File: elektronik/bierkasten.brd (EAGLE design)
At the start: 160 x 100 mm, 71 parts, among them Q1 BC547B

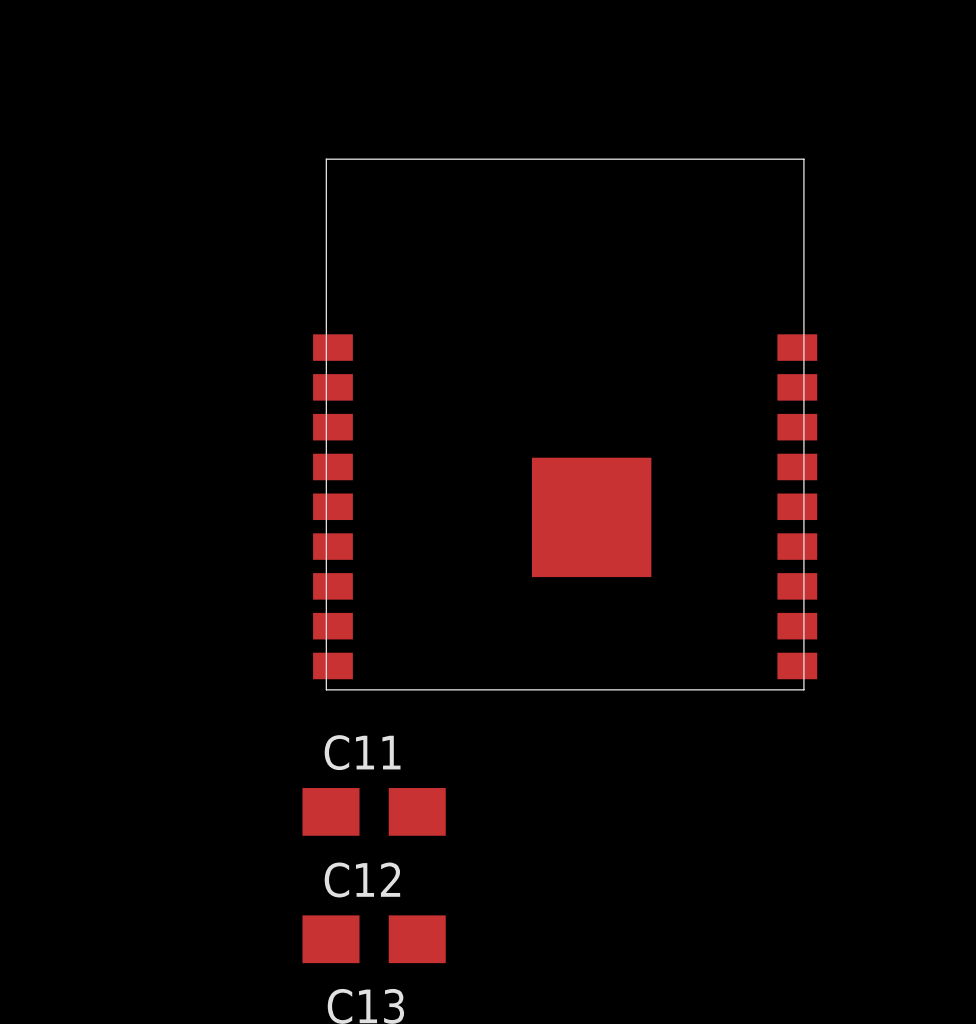
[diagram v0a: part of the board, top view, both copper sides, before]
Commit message: Bestellcodes fertig gemacht
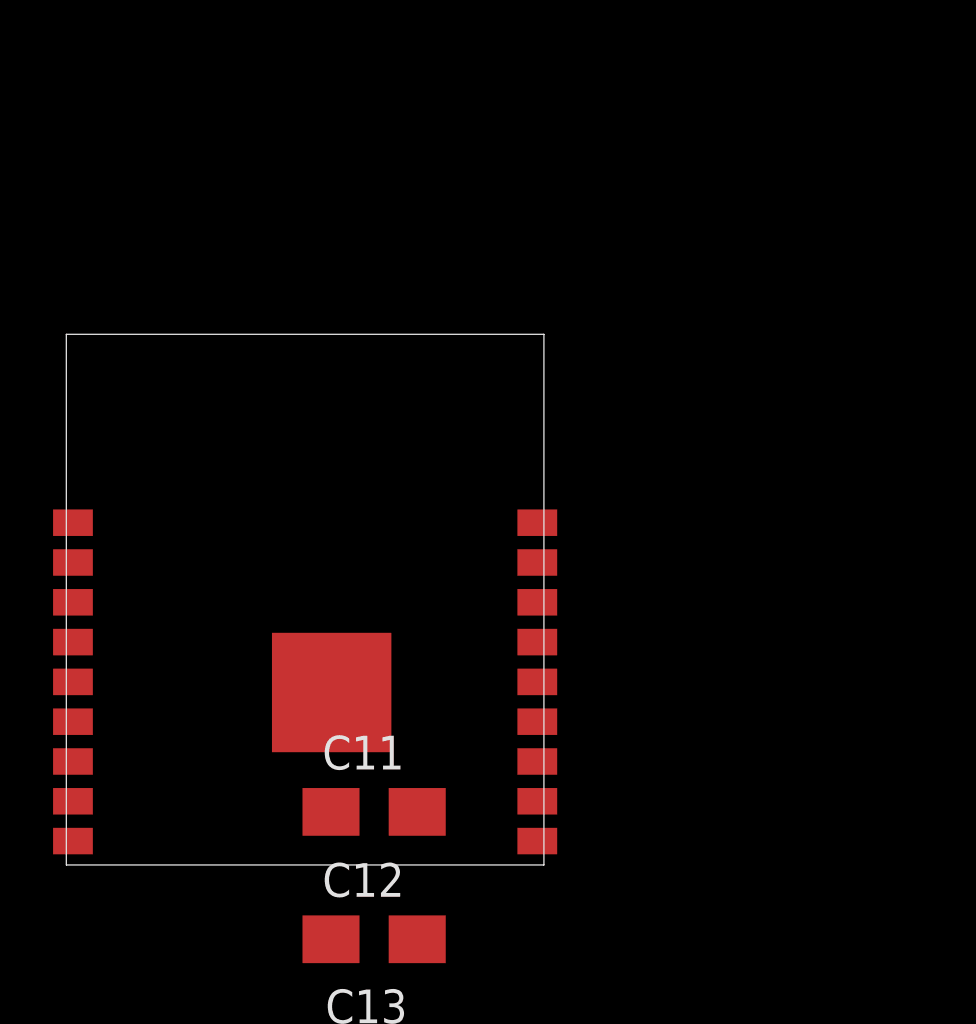
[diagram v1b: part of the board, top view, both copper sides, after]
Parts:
- added U$17: BESTELLTEILE, misc_STE:BESTELLTEILE
- C11, C12: value 10u -> 10u/20V
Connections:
- net +3V3: now also C11.+
- net GND: now also C11.-
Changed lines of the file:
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@@
 <attribute name="SPICEPREFIX" value="C" x="22.2" y="48.2" size="1.778" layer="27" display="off"/>
 </element>
-<element name="FERRITE1" library="ferrite_STE" package="L0805" value="" x="-4" y="48.2"/>
+<element name="FERRITE1" library="ferrite_STE" package="L0805" value="" x="-4" y="48.2">
+<attribute name="REICHELT" value="BLM21PG 331" x="-4" y="48.2" size="1.778" layer="27" display="off"/>
+</element>
 <element name="LD1" library="opto_STE" package="DUOLED-C-WIRE" value="" x="29.8" y="38.6" rot="R90">
 <attribute name="REICHELT" value="LED 5 RG-3" x="29.8" y="38.6" size="1.778" layer="27" rot="R90" display="off"/>
@@
 <attribute name="SPICEPREFIX" value="R" x="47.2" y="66" size="1.778" layer="27" display="off"/>
 </element>
-<element name="Q1" library="transistor-npn" library_urn="urn:adsk.eagle:library:398" package="TO92" package3d_urn="urn:adsk.eagle:package:28523/2" value="BC547B" x="90" y="105.2"/>
+<element name="Q1" library="transistor-npn" library_urn="urn:adsk.eagle:library:398" package="TO92" package3d_urn="urn:adsk.eagle:package:28523/2" value="BC547B" x="90" y="105.2">
+<attribute name="REICHELT" value="BC 547B" x="90" y="105.2" size="1.778" layer="27" display="off"/>
+</element>
 <element name="U$3" library="misc_STE" package="LPT80" value="LPT80" x="88.8" y="92.4">
 <attribute name="REICHELT" value="LPT 80" x="88.8" y="92.4" size="1.778" layer="27" display="off"/>
@@
 <attribute name="WUERTH" value="430 182 043 816" x="-54.8" y="78.6" size="1.778" layer="27" display="off"/>
 </element>
-<element name="U$15" library="misc_STE" package="ESP8266-POLLIN" value="ESP8266-POLLIN" x="-79" y="0.2"/>
-<element name="C11" library="rcl" library_urn="urn:adsk.eagle:library:334" package="B/3528-21W" package3d_urn="urn:adsk.eagle:package:23411/1" value="10u" x="-77.2" y="-4.4">
+<element name="U$15" library="misc_STE" package="ESP8266-POLLIN" value="ESP8266-POLLIN" x="-79" y="0.2">
+<attribute name="NOORDER" value="" x="-79" y="0.2" size="1.778" layer="27" display="off"/>
+</element>
+<element name="C11" library="rcl" library_urn="urn:adsk.eagle:library:334" package="B/3528-21W" package3d_urn="urn:adsk.eagle:package:23411/1" value="10u/20V" x="-77.2" y="-4.4">
+<attribute name="REICHELT" value="TAJ 3528 10/20" x="-77.2" y="-4.4" size="1.778" layer="27" display="off"/>
 <attribute name="SPICEPREFIX" value="C" x="-77.2" y="-4.4" size="1.778" layer="27" display="off"/>
 </element>
-<element name="C12" library="rcl" library_urn="urn:adsk.eagle:library:334" package="B/3528-21W" package3d_urn="urn:adsk.eagle:package:23411/1" value="10u" x="-77.2" y="-9.2">
+<element name="C12" library="rcl" library_urn="urn:adsk.eagle:library:334" package="B/3528-21W" package3d_urn="urn:adsk.eagle:package:23411/1" value="10u/20V" x="-77.2" y="-9.2">
+<attribute name="REICHELT" value="TAJ 3528 10/20" x="-77.2" y="-9.2" size="1.778" layer="27" display="off"/>
 <attribute name="SPICEPREFIX" value="C" x="-77.2" y="-9.2" size="1.778" layer="27" display="off"/>
 </element>
@@
 <attribute name="SPICEPREFIX" value="C" x="-78.4" y="-21.6" size="1.778" layer="27" display="off"/>
 </element>
-<element name="JP1" library="jumper" library_urn="urn:adsk.eagle:library:252" package="JP2" package3d_urn="urn:adsk.eagle:package:15452/1" value="" x="-84" y="-22.6"/>
+<element name="JP1" library="jumper" library_urn="urn:adsk.eagle:library:252" package="JP2" package3d_urn="urn:adsk.eagle:package:15452/1" value="" x="-84" y="-22.6">
+<attribute name="NOORDER" value="" x="-84" y="-22.6" size="1.778" layer="27" display="off"/>
+</element>
 <element name="R25" library="rcl" library_urn="urn:adsk.eagle:library:334" package="R0603" package3d_urn="urn:adsk.eagle:package:23555/2" value="10k" x="-86.4" y="-28.4">
+<attribute name="FARNELL" value="2502397" x="-86.4" y="-28.4" size="1.778" layer="27" display="off"/>
+<attribute name="REICHELT" value="RND 0603 1 10K" x="-86.4" y="-28.4" size="1.778" layer="27" display="off"/>
 <attribute name="SPICEPREFIX" value="R" x="-86.4" y="-28.4" size="1.778" layer="27" display="off"/>
 </element>
 <element name="R26" library="rcl" library_urn="urn:adsk.eagle:library:334" package="R0603" package3d_urn="urn:adsk.eagle:package:23555/2" value="10k" x="-86.4" y="-33.4">
+<attribute name="FARNELL" value="2502397" x="-86.4" y="-33.4" size="1.778" layer="27" display="off"/>
+<attribute name="REICHELT" value="RND 0603 1 10K" x="-86.4" y="-33.4" size="1.778" layer="27" display="off"/>
 <attribute name="SPICEPREFIX" value="R" x="-86.4" y="-33.4" size="1.778" layer="27" display="off"/>
 </element>
 <element name="R27" library="rcl" library_urn="urn:adsk.eagle:library:334" package="R0603" package3d_urn="urn:adsk.eagle:package:23555/2" value="10k" x="-86.4" y="-38.4">
+<attribute name="FARNELL" value="2502397" x="-86.4" y="-38.4" size="1.778" layer="27" display="off"/>
+<attribute name="REICHELT" value="RND 0603 1 10K" x="-86.4" y="-38.4" size="1.778" layer="27" display="off"/>
 <attribute name="SPICEPREFIX" value="R" x="-86.4" y="-38.4" size="1.778" layer="27" display="off"/>
+</element>
+<element name="U$17" library="misc_STE" package="BESTELLTEILE" value="BESTELLTEILE" x="-89" y="-41.4">
+<attribute name="REICHELT" value="SL 1X36G 2,54:JUMPER 2,54 GN*10" x="-89" y="-41.4" size="1.778" layer="27" display="off"/>
 </element>
 </elements>
@@
 <wire x1="33.0024" y1="41.52525625" x2="33.0024" y2="39.9524" width="0.3" layer="1"/>
 <wire x1="33.0024" y1="39.9524" x2="32.2" y2="39.15" width="0.3" layer="1"/>
+<contactref element="C11" pad="+"/>
 <wire x1="84.45" y1="78.4" x2="90.07" y2="92.4" width="0" layer="19" extent="1-1"/>
 <wire x1="43.45" y1="52.2" x2="84.45" y2="78.4" width="0" layer="19" extent="1-1"/>
@@
 <wire x1="19.06" y1="67.47" x2="26.7976" y2="60.4476" width="0" layer="19" extent="1-1"/>
 <wire x1="-4.95" y1="48.2" x2="21.35" y2="51.8" width="0" layer="19" extent="1-1"/>
+<wire x1="-75.575" y1="-4.4" x2="-4.95" y2="48.2" width="0" layer="19" extent="1-1"/>
 </signal>
 <signal name="GND">
@@
 <contactref element="R27" pad="1"/>
 <contactref element="JP1" pad="1"/>
+<contactref element="C11" pad="-"/>
 <wire x1="75.8" y1="120.67" x2="88.4" y2="120.67" width="0" layer="19" extent="1-1"/>
 <wire x1="63" y1="120.67" x2="75.8" y2="120.67" width="0" layer="19" extent="1-1"/>
@@
 <wire x1="-50.3" y1="80.85" x2="-38.6" y2="120.67" width="0" layer="19" extent="1-1"/>
 <wire x1="-59.3" y1="80.85" x2="-50.3" y2="80.85" width="0" layer="19" extent="1-1"/>
-<wire x1="-61.25" y1="13.1" x2="-59.3" y2="80.85" width="0" layer="19" extent="1-1"/>
-<wire x1="-61.25" y1="5.6" x2="-61.25" y2="13.1" width="0" layer="19" extent="1-1"/>
-<wire x1="-69" y1="6.7" x2="-61.25" y2="5.6" width="0" layer="19" extent="1-1"/>
-<wire x1="-78.75" y1="1.1" x2="-69" y2="6.7" width="0" layer="19" extent="1-1"/>
-<wire x1="-78.825" y1="-9.2" x2="-78.75" y2="1.1" width="0" layer="19" extent="1-1"/>
+<wire x1="-71.05" y1="6.5" x2="-59.3" y2="80.85" width="0" layer="19" extent="1-1"/>
+<wire x1="-71.05" y1="-1" x2="-71.05" y2="6.5" width="0" layer="19" extent="1-1"/>
+<wire x1="-78.8" y1="0.1" x2="-71.05" y2="-1" width="0" layer="19" extent="1-1"/>
+<wire x1="-88.55" y1="-5.5" x2="-78.8" y2="0.1" width="0" layer="19" extent="1-1"/>
+<wire x1="-78.825" y1="-4.4" x2="-88.55" y2="-5.5" width="0" layer="19" extent="1-1"/>
+<wire x1="-78.825" y1="-9.2" x2="-78.825" y2="-4.4" width="0" layer="19" extent="1-1"/>
 <wire x1="-77.55" y1="-13" x2="-78.825" y2="-9.2" width="0" layer="19" extent="1-1"/>
 <wire x1="-79.25" y1="-21.6" x2="-77.55" y2="-13" width="0" layer="19" extent="1-1"/>
@@
 <contactref element="R25" pad="1"/>
 <wire x1="-77.55" y1="-21.6" x2="-87.25" y2="-28.4" width="0" layer="19" extent="1-1"/>
-<wire x1="-78.75" y1="11.6" x2="-77.55" y2="-21.6" width="0" layer="19" extent="1-1"/>
+<wire x1="-88.55" y1="5" x2="-77.55" y2="-21.6" width="0" layer="19" extent="1-1"/>
 </signal>
 <signal name="N$25">
 <contactref element="U$15" pad="6"/>
 <contactref element="R27" pad="2"/>
-<wire x1="-78.75" y1="5.6" x2="-85.55" y2="-38.4" width="0" layer="19" extent="1-1"/>
+<wire x1="-88.55" y1="-1" x2="-85.55" y2="-38.4" width="0" layer="19" extent="1-1"/>
 </signal>
 <signal name="WIFI_RXD">
 <contactref element="U$15" pad="12"/>
 <contactref element="U$1" pad="31"/>
-<wire x1="-61.25" y1="4.1" x2="40.15" y2="46.7" width="0" layer="19" extent="1-1"/>
+<wire x1="-71.05" y1="-2.5" x2="40.15" y2="46.7" width="0" layer="19" extent="1-1"/>
 </signal>
 <signal name="WIFI_TXD">
 <contactref element="U$15" pad="11"/>
 <contactref element="U$1" pad="32"/>
-<wire x1="-61.25" y1="2.6" x2="40.15" y2="47.2" width="0" layer="19" extent="1-1"/>
+<wire x1="-71.05" y1="-4" x2="40.15" y2="47.2" width="0" layer="19" extent="1-1"/>
 </signal>
 <signal name="WIFI_BOOT">
 <contactref element="U$15" pad="8"/>
 <contactref element="JP1" pad="2"/>
-<wire x1="-78.75" y1="2.6" x2="-84" y2="-22.6" width="0" layer="19" extent="1-1"/>
+<wire x1="-88.55" y1="-4" x2="-84" y2="-22.6" width="0" layer="19" extent="1-1"/>
 </signal>
 <signal name="+UB">
@@
 <wire x1="-79.25" y1="-13" x2="-81.46" y2="-22.6" width="0" layer="19" extent="1-1"/>
 <wire x1="-75.575" y1="-9.2" x2="-79.25" y2="-13" width="0" layer="19" extent="1-1"/>
-<wire x1="-78.75" y1="13.1" x2="-75.575" y2="-9.2" width="0" layer="19" extent="1-1"/>
+<wire x1="-88.55" y1="6.5" x2="-75.575" y2="-9.2" width="0" layer="19" extent="1-1"/>
 </signal>
 <signal name="N$26">
 <contactref element="U$15" pad="15"/>
 <contactref element="R26" pad="1"/>
-<wire x1="-61.25" y1="8.6" x2="-87.25" y2="-33.4" width="0" layer="19" extent="1-1"/>
+<wire x1="-71.05" y1="2" x2="-87.25" y2="-33.4" width="0" layer="19" extent="1-1"/>
 </signal>
 </signals>

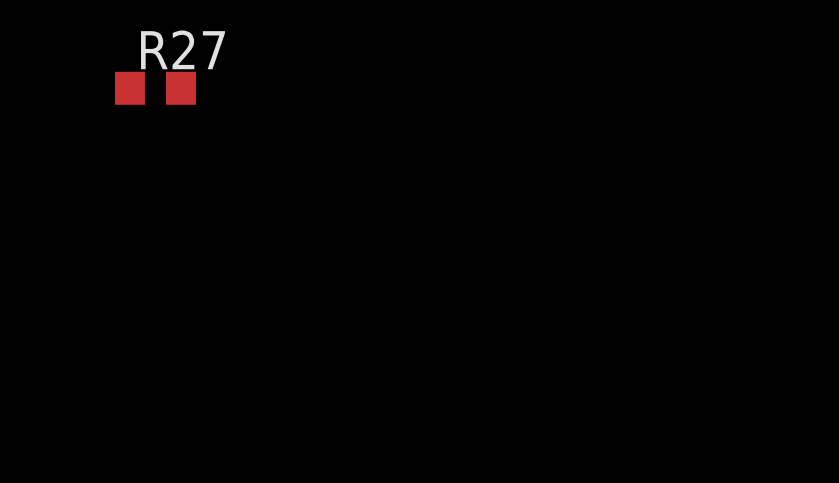
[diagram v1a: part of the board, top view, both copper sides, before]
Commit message: Stecker für User-Wahlschalter hinzugefügt.
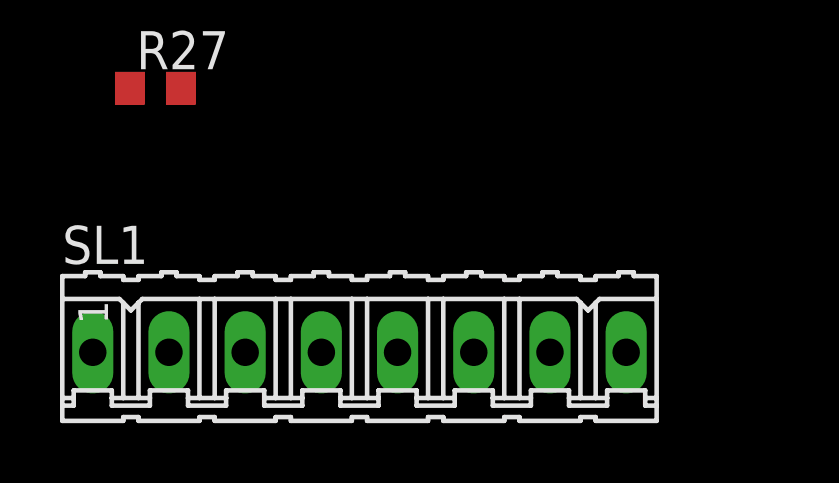
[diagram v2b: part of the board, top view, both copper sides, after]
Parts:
- added SL1: (no value), con-amp-quick:08P
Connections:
- new net USER_0: SL1.2, U$1.95
- new net USER_1: SL1.3, U$1.96
- new net USER_2: SL1.4, U$1.97
- new net USER_3: SL1.5, U$1.98
- new net USER_4: SL1.6, U$1.99
- new net USER_5: SL1.7, U$1.100
- new net USER_COMMON: SL1.1
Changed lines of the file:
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@@
 <attribute name="REICHELT" value="SL 1X36G 2,54:JUMPER 2,54 GN*10" x="-89" y="-41.4" size="1.778" layer="27" display="off"/>
+</element>
+<element name="SL1" library="con-amp-quick" library_urn="urn:adsk.eagle:library:125" package="08P" package3d_urn="urn:adsk.eagle:package:5962/1" value="" x="-79.6" y="-47.2">
+<attribute name="MF" value="" x="-79.6" y="-47.2" size="1.778" layer="27" display="off"/>
+<attribute name="MPN" value="" x="-79.6" y="-47.2" size="1.778" layer="27" display="off"/>
+<attribute name="OC_FARNELL" value="unknown" x="-79.6" y="-47.2" size="1.778" layer="27" display="off"/>
+<attribute name="OC_NEWARK" value="unknown" x="-79.6" y="-47.2" size="1.778" layer="27" display="off"/>
 </element>
 </elements>
@@
 <wire x1="-71.05" y1="2" x2="-87.25" y2="-33.4" width="0" layer="19" extent="1-1"/>
 </signal>
+<signal name="USER_5">
+<contactref element="SL1" pad="7"/>
+<contactref element="U$1" pad="100"/>
+<wire x1="24.65" y1="44.2" x2="-73.25" y2="-47.2" width="0" layer="19" extent="1-1"/>
+</signal>
+<signal name="USER_4">
+<contactref element="SL1" pad="6"/>
+<contactref element="U$1" pad="99"/>
+<wire x1="24.65" y1="44.7" x2="-75.79" y2="-47.2" width="0" layer="19" extent="1-1"/>
+</signal>
+<signal name="USER_3">
+<contactref element="SL1" pad="5"/>
+<contactref element="U$1" pad="98"/>
+<wire x1="24.65" y1="45.2" x2="-78.33" y2="-47.2" width="0" layer="19" extent="1-1"/>
+</signal>
+<signal name="USER_2">
+<contactref element="SL1" pad="4"/>
+<contactref element="U$1" pad="97"/>
+<wire x1="24.65" y1="45.7" x2="-80.87" y2="-47.2" width="0" layer="19" extent="1-1"/>
+</signal>
+<signal name="USER_1">
+<contactref element="SL1" pad="3"/>
+<contactref element="U$1" pad="96"/>
+<wire x1="24.65" y1="46.2" x2="-83.41" y2="-47.2" width="0" layer="19" extent="1-1"/>
+</signal>
+<signal name="USER_0">
+<contactref element="SL1" pad="2"/>
+<contactref element="U$1" pad="95"/>
+<wire x1="24.65" y1="46.7" x2="-85.95" y2="-47.2" width="0" layer="19" extent="1-1"/>
+</signal>
+<signal name="USER_COMMON">
+<contactref element="SL1" pad="1"/>
+</signal>
 </signals>

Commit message: Schaltplan fertig
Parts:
- added C15: 100n, rcl_STE:C0603
- added C16: 10u/20V, rcl:B/3528-21W
- added Q2: NXP2301P-SOT23, mosfet_STE:SOT23
- added R28: 10k, rcl:R0603
- added SL2: (no value), con-amp-quick:02P
- added U$16: NCP1117ST33T3G, power_STE:SOT223
- U$10, U$11, U$12, U$13, U$14, U$4, U$5, U$6, U$7, U$8, U$9: value SWITCH_SINGLE-WIRED -> ESE11HS2
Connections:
- removed net USER_COMMON: SL1.1
- new net BATTERY: SL2.2, U$16.3
- new net WIFI_ENABLE: Q2.1, R28.1, U$1.2
- net +3V3: now also C15.1, C16.+, Q2.2, R28.2, SL1.1, U$16.2, U$16.4
- net +UB: now also Q2.3
- net GND: now also C15.2, C16.-, SL2.1, U$16.1

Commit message: Layout fertig
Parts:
- added C17: 100n, rcl_STE:C0603
- added C18: 10u/20V, rcl:B/3528-21W
- moved U$17 252.6 mm to (160.2, 0.00), flipped to the bottom
- moved SL2 146.3 mm to (3.40, 33.2), flipped to the bottom
- moved C16 144.6 mm to (9.00, 32.2), flipped to the bottom, turned to 180 degrees
- moved C15 143.4 mm to (9.60, 34.4), flipped to the bottom
- moved U$16 141.6 mm to (11.4, 39.0), flipped to the bottom, turned to 90 degrees
- moved SL1 139.6 mm to (30.8, 38.2), turned to 180 degrees
- moved U$14 130.0 mm to (23.0, 4.90), flipped to the bottom, turned to 180 degrees
- moved U$4 123.8 mm to (32.0, 9.20), flipped to the bottom, turned to 0 degrees
- moved U$13 123.4 mm to (23.0, 6.15), flipped to the bottom, turned to 180 degrees
- moved R28 121.0 mm to (14.8, 6.40), flipped to the bottom, turned to 270 degrees
- moved U$5 119.9 mm to (32.0, 7.80), flipped to the bottom, turned to 0 degrees
- moved U$6 119.1 mm to (33.4, 4.00), flipped to the bottom, turned to 90 degrees
- moved U$11 118.5 mm to (26.4, 4.00), flipped to the bottom, turned to 90 degrees
- moved U$12 117.8 mm to (23.2, 7.40), flipped to the bottom, turned to 180 degrees
- moved U$7 116.8 mm to (32.0, 4.00), flipped to the bottom, turned to 90 degrees
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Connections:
- net BATTERY: now also C17.1, C18.+
- net GND: now also C17.2, C18.-
- net WIFI_ENABLE: now also U$1.81; no longer U$1.2
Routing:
- net +3V3: track 29.5 -> 168.5 mm, vias 0 -> 6
- net GND: track 15.6 -> 97.2 mm, vias 0 -> 37
- net !RESET: track 0.00 -> 52.9 mm, vias 0 -> 1
- net USER_0: track 0.00 -> 32.5 mm, vias 0 -> 1
- net TDO: track 0.00 -> 31.3 mm, vias 0 -> 1
- net USER_1: track 0.00 -> 29.6 mm, vias 0 -> 1
- net TDI: track 0.00 -> 26.8 mm
- net USER_2: track 0.00 -> 26.3 mm, vias 0 -> 1
- net +UB: track 0.00 -> 24.2 mm, vias 0 -> 1
- net TCK: track 0.00 -> 24.1 mm
- net USER_3: track 0.00 -> 23.6 mm, vias 0 -> 1
- net SWITCH_10: track 0.00 -> 21.3 mm, vias 0 -> 1
- net N$1: track 0.00 -> 21.0 mm
- net SWITCH_7: track 0.00 -> 20.9 mm, vias 0 -> 1
- net USER_4: track 0.00 -> 20.9 mm, vias 0 -> 1
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- added copper zone on layer 16, net +3V3
- added copper zone on layer 1, net GND
- added copper zone on layer 16, net GND
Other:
- board size 160 x 100 mm -> 41 x 51 mm
